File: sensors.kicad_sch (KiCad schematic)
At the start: 3 parts, among them IC5 BME690, U2 BME280, U3 BMP581

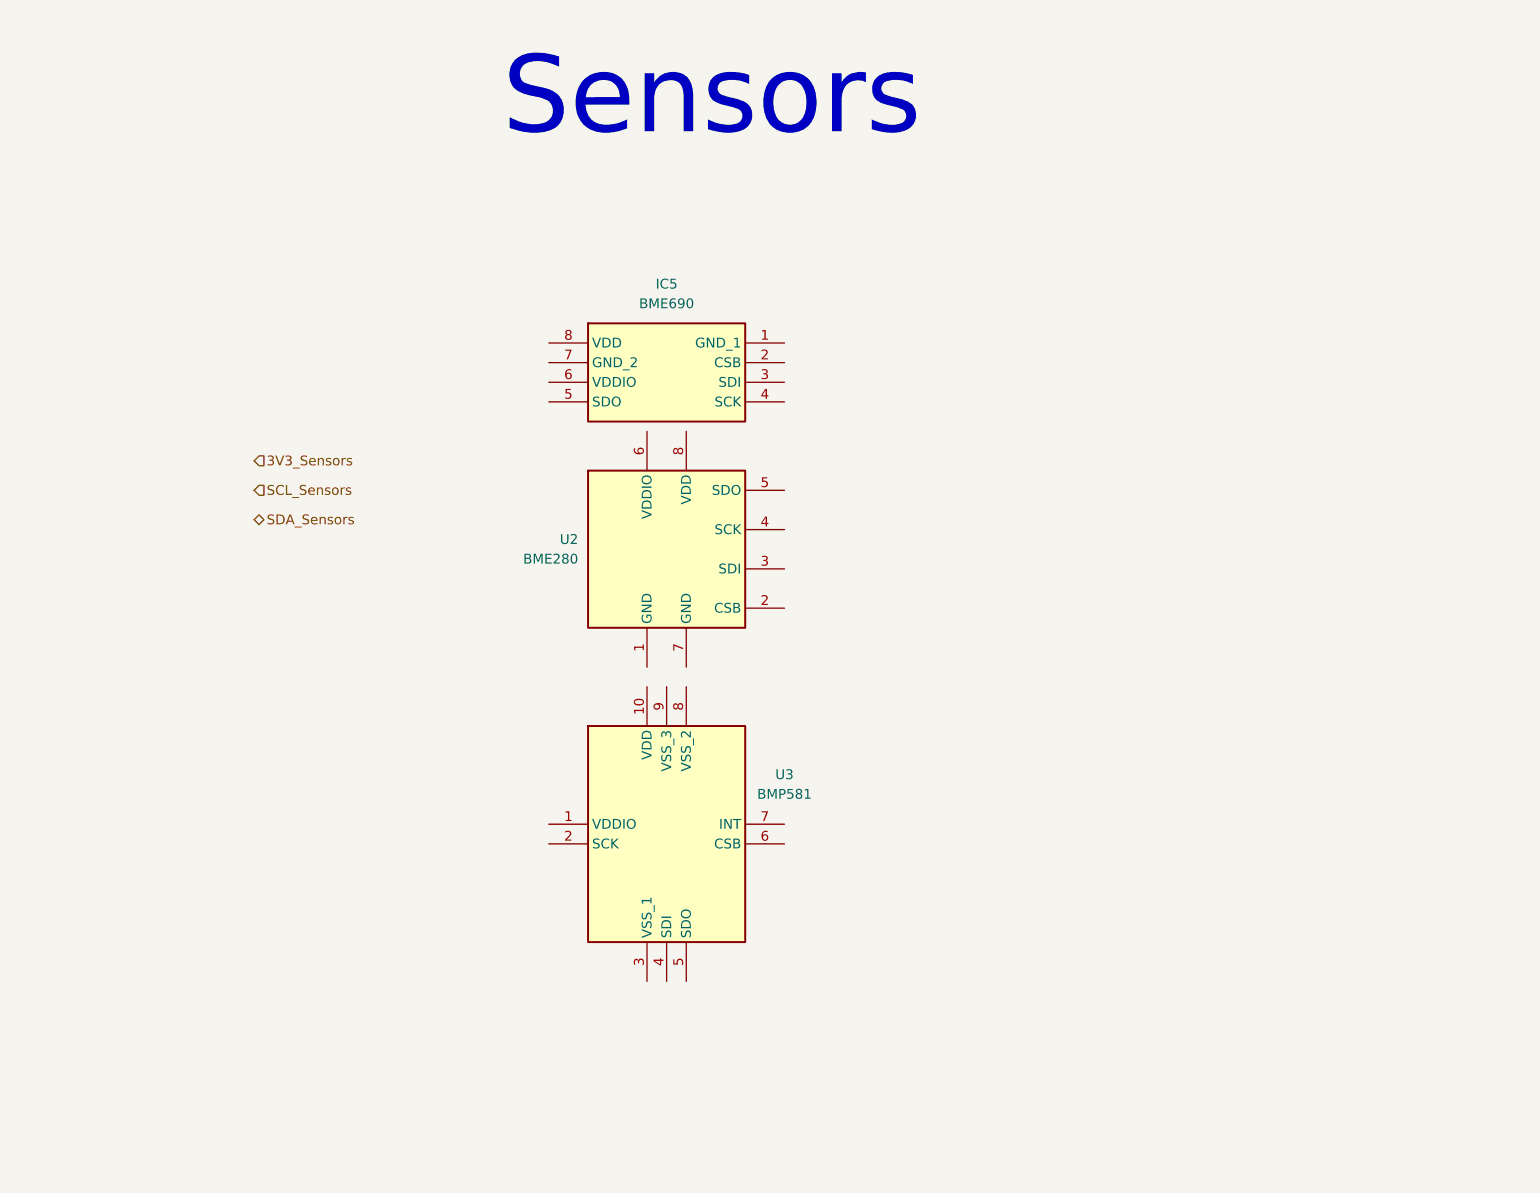
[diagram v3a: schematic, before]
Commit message: Cable all sensors
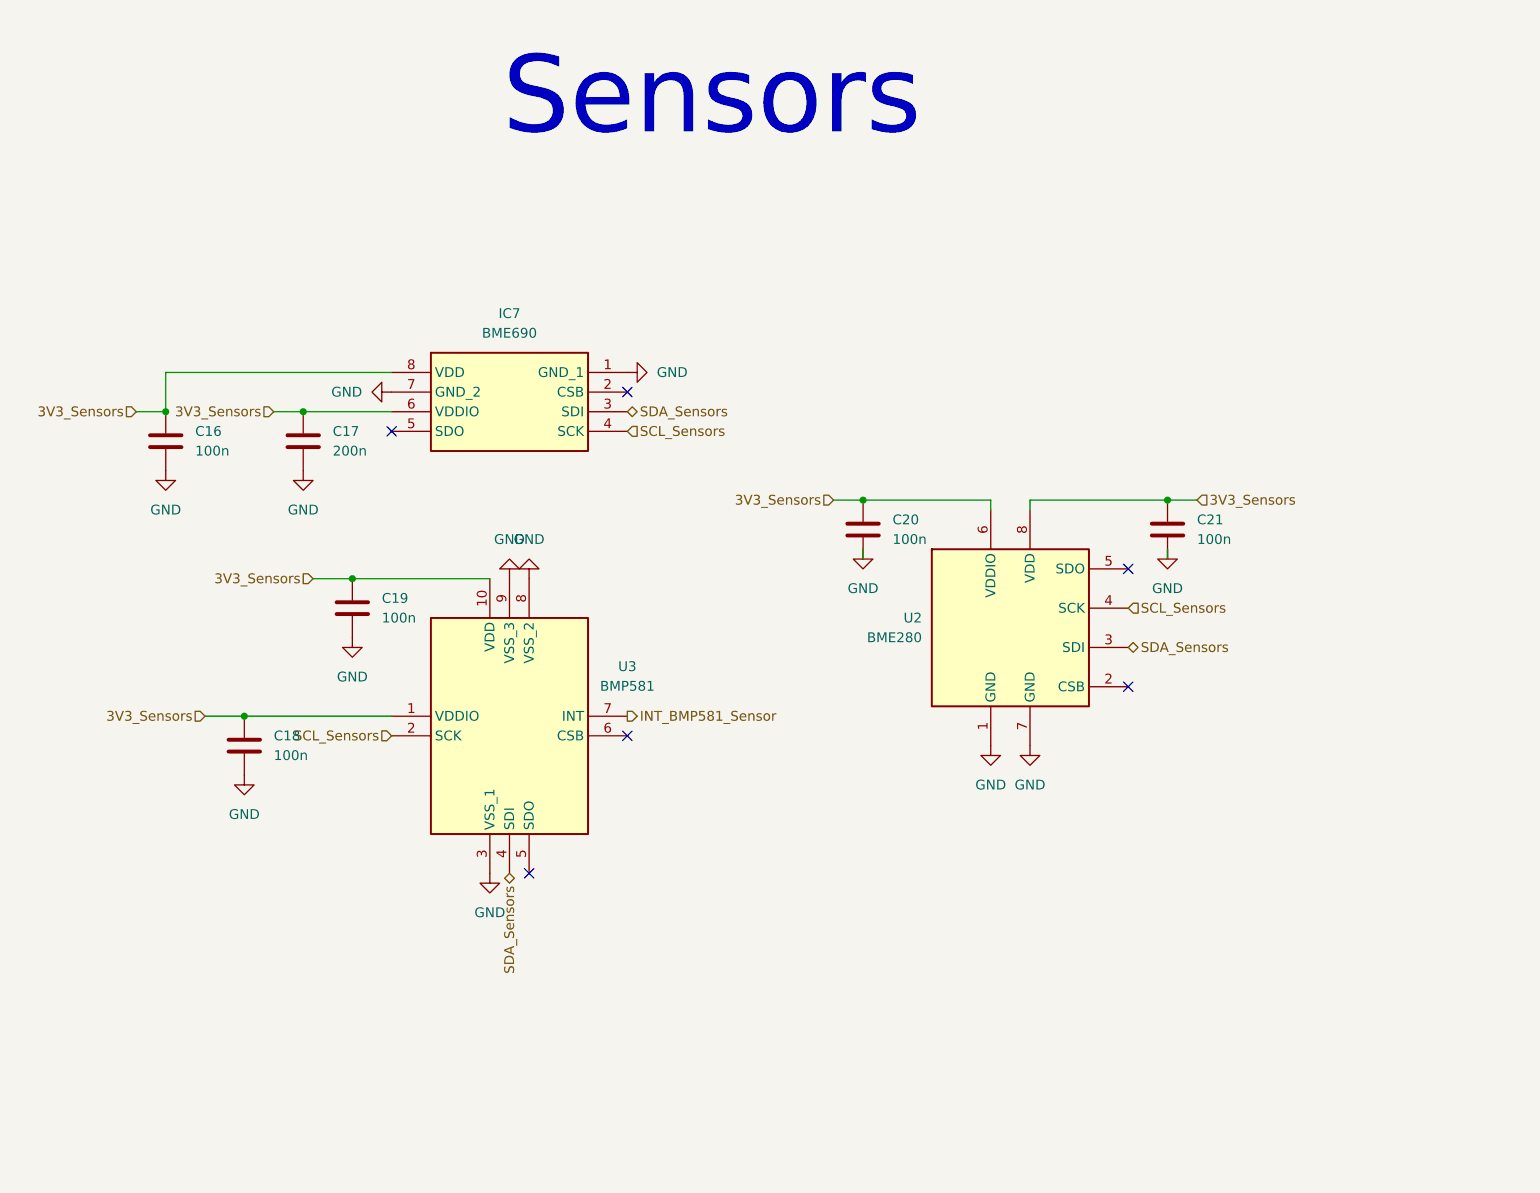
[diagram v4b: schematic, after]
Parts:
- removed IC5: BME690, BME690, symbol weather-station-poc-sym:BME690
- added C16, C18, C19, C20, C21: 100n, Capacitor_SMD:C_0402_1005Metric_Pad0.74x0.62mm_HandSolder, symbol Device:C
- added C17: 200n, Capacitor_SMD:C_0402_1005Metric_Pad0.74x0.62mm_HandSolder, symbol Device:C
- added IC7: BME690, BME690, symbol weather-station-poc-sym:BME690
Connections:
- net 3V3_Sensors: now also U2.6 (VDDIO), U2.8 (VDD), U3.1 (VDDIO), U3.10 (VDD), C16.1, C17.1, C18.1, C19.1, C20.1, C21.1, IC7.6 (VDDIO), IC7.8 (VDD)
- net SCL_Sensors: now also U2.4 (SCK), U3.2 (SCK), IC7.4 (SCK)
- net SDA_Sensors: now also U2.3 (SDI), U3.4 (SDI), IC7.3 (SDI)
- net GND: now reaches U3.3 (VSS_1)
- net GND: now also U2.1 (GND), U2.7 (GND), U3.8 (VSS_2), U3.9 (VSS_3), C16.2, C17.2, C18.2, C19.2, C20.2, C21.2, IC7.1 (GND_1), IC7.7 (GND_2)
- net INT_BMP581_Sensor: now reaches U3.7 (INT)
- no-connect marks 0 -> 6
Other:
- moved on the sheet: U2, U3

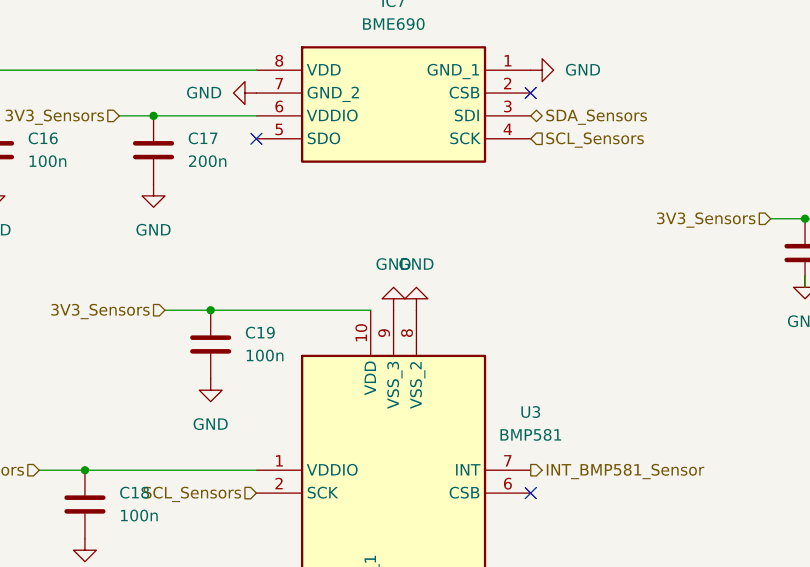
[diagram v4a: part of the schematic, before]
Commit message: Add S2LP schematic
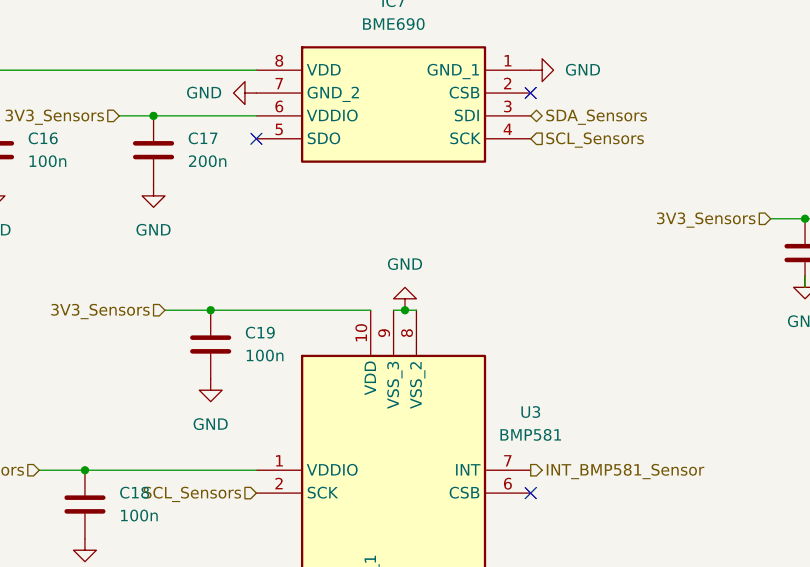
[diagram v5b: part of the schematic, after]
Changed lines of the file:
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@@
+	)
+	(junction
+		(at 124.46 88.9)
+		(diameter 0)
+		(color 0 0 0 0)
 	)
 	(junction
@@
 	(wire
 		(pts
+			(xy 124.46 88.9) (xy 125.73 88.9)
+		)
+		(stroke
+			(width 0)
+			(type default)
+		)
+	)
+	(wire
+		(pts
 			(xy 78.74 67.31) (xy 78.74 62.23)
 		)
@@
 		(pts
 			(xy 102.87 88.9) (xy 120.65 88.9)
+		)
+		(stroke
+			(width 0)
+			(type default)
+		)
+	)
+	(wire
+		(pts
+			(xy 123.19 88.9) (xy 124.46 88.9)
 		)
 		(stroke
@@
 	(symbol
 		(lib_id "power:GND")
-		(at 125.73 88.9 180)
-		(unit 1)
-		(exclude_from_sim no)
-		(in_bom yes)
-		(on_board yes)
-		(dnp no)
-		(fields_autoplaced yes)
-		(property "Reference" "#PWR043"
-			(at 125.73 82.55 0)
-			(effects
-				(font
-					(size 1.27 1.27)
-				)
-				(hide yes)
-			)
-		)
-		(property "Value" "GND"
-			(at 125.73 83.82 0)
-			(effects
-				(font
-					(size 1.27 1.27)
-				)
-			)
-		)
-		(property "Footprint" ""
-			(at 125.73 88.9 0)
-			(effects
-				(font
-					(size 1.27 1.27)
-				)
-				(hide yes)
-			)
-		)
-		(property "Datasheet" ""
-			(at 125.73 88.9 0)
-			(effects
-				(font
-					(size 1.27 1.27)
-				)
-				(hide yes)
-			)
-		)
-		(property "Description" "Power symbol creates a global label with name \"GND\" , ground"
-			(at 125.73 88.9 0)
-			(effects
-				(font
-					(size 1.27 1.27)
-				)
-				(hide yes)
-			)
-		)
-		(pin "1"
-		)
-		(instances
-			(project "weather-station-poc"
-				(path "/38eb53bb-294e-46e4-ad59-fd355ca373b9/29574217-d56b-4a63-a2c4-128dfec2758e"
-					(reference "#PWR043")
-					(unit 1)
-				)
-			)
-		)
-	)
-	(symbol
-		(lib_id "power:GND")
 		(at 190.5 110.49 0)
 		(unit 1)
@@
 	(symbol
 		(lib_id "power:GND")
-		(at 123.19 88.9 180)
+		(at 124.46 88.9 180)
 		(unit 1)
 		(exclude_from_sim no)
@@
 		(fields_autoplaced yes)
 		(property "Reference" "#PWR042"
-			(at 123.19 82.55 0)
+			(at 124.46 82.55 0)
 			(effects
 				(font
@@
 		)
 		(property "Value" "GND"
-			(at 123.19 83.82 0)
+			(at 124.46 83.82 0)
 			(effects
 				(font
@@
 		)
 		(property "Footprint" ""
-			(at 123.19 88.9 0)
+			(at 124.46 88.9 0)
 			(effects
 				(font
@@
 		)
 		(property "Datasheet" ""
-			(at 123.19 88.9 0)
+			(at 124.46 88.9 0)
 			(effects
 				(font
@@
 		)
 		(property "Description" "Power symbol creates a global label with name \"GND\" , ground"
-			(at 123.19 88.9 0)
-			(effects
-				(font
+			(at 124.46 88.9 0)
+			(effects
+				(font

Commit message: Fix warnings for footprint
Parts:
- IC7: footprint BME690 -> weather-station-poc-fp:BME690
- U3: footprint BMP581 -> weather-station-poc-fp:BMP581
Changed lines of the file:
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@@
 			)
 		)
-		(property "Footprint" "BMP581"
+		(property "Footprint" "weather-station-poc-fp:BMP581"
 			(at 134.62 191.44 0)
 			(effects
@@
 			)
 		)
-		(property "Footprint" "BME690"
+		(property "Footprint" "weather-station-poc-fp:BME690"
 			(at 134.62 157.15 0)
 			(effects

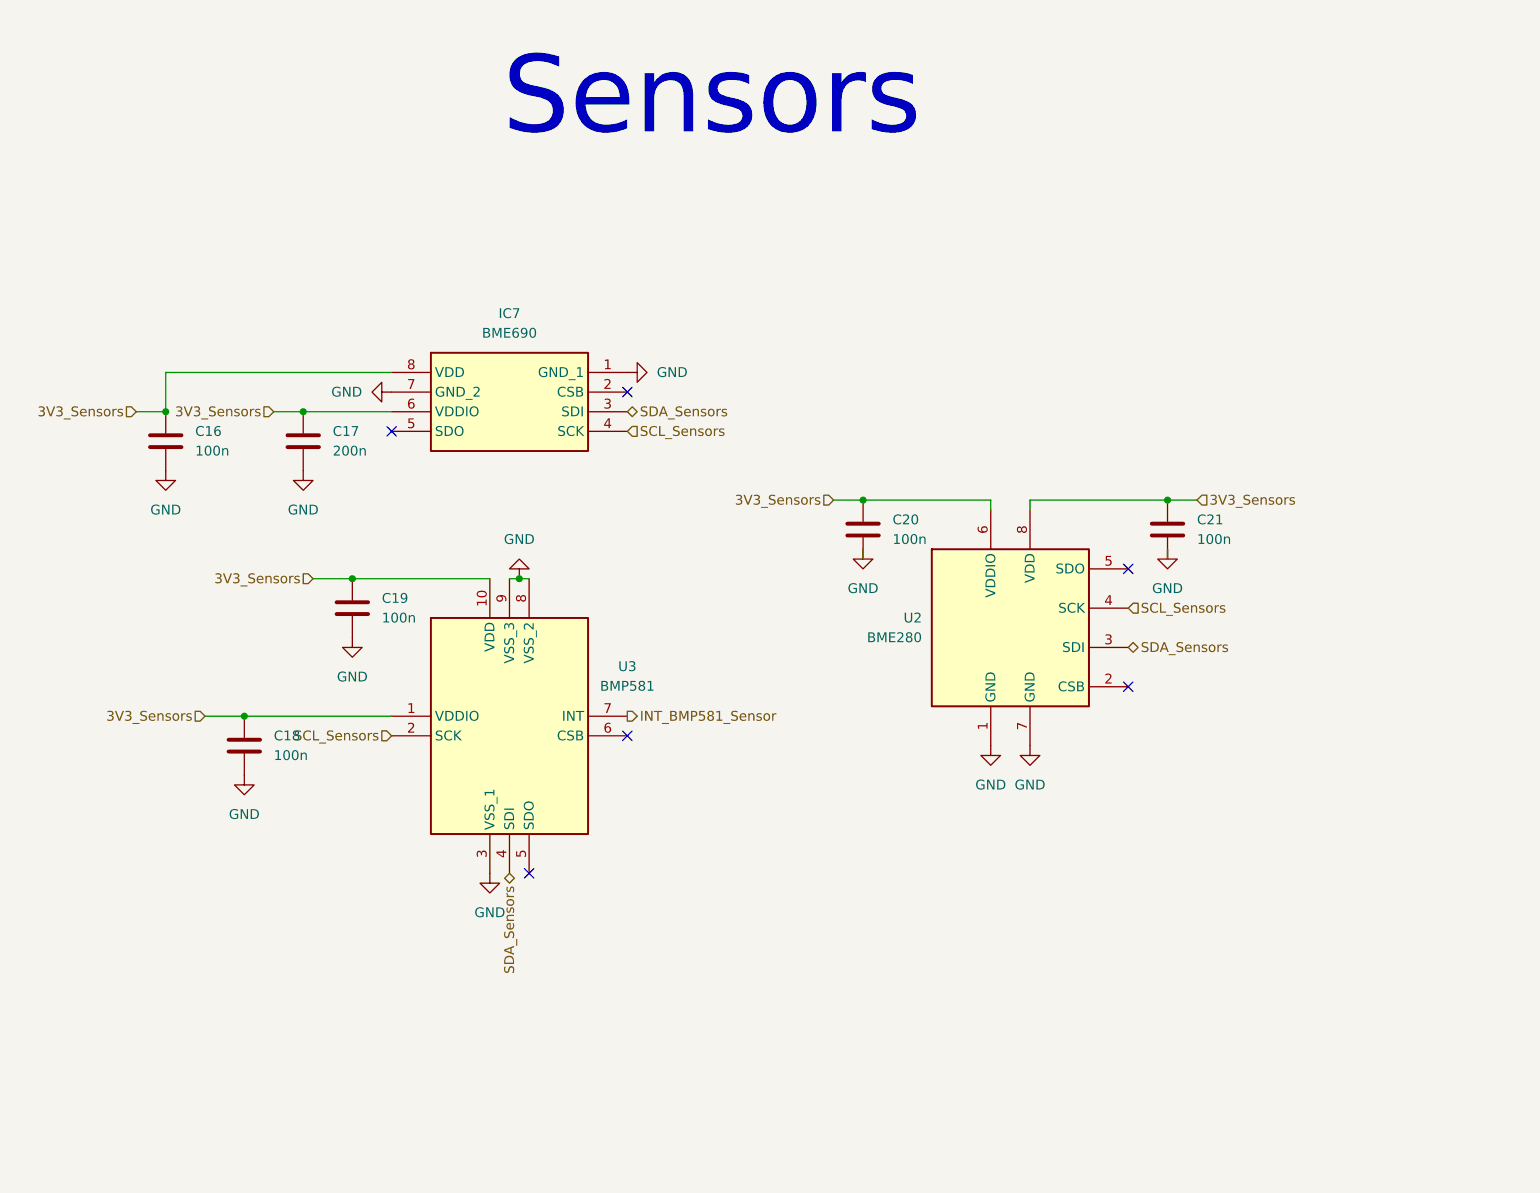
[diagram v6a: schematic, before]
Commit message: Functionnal block delimiting in schematics
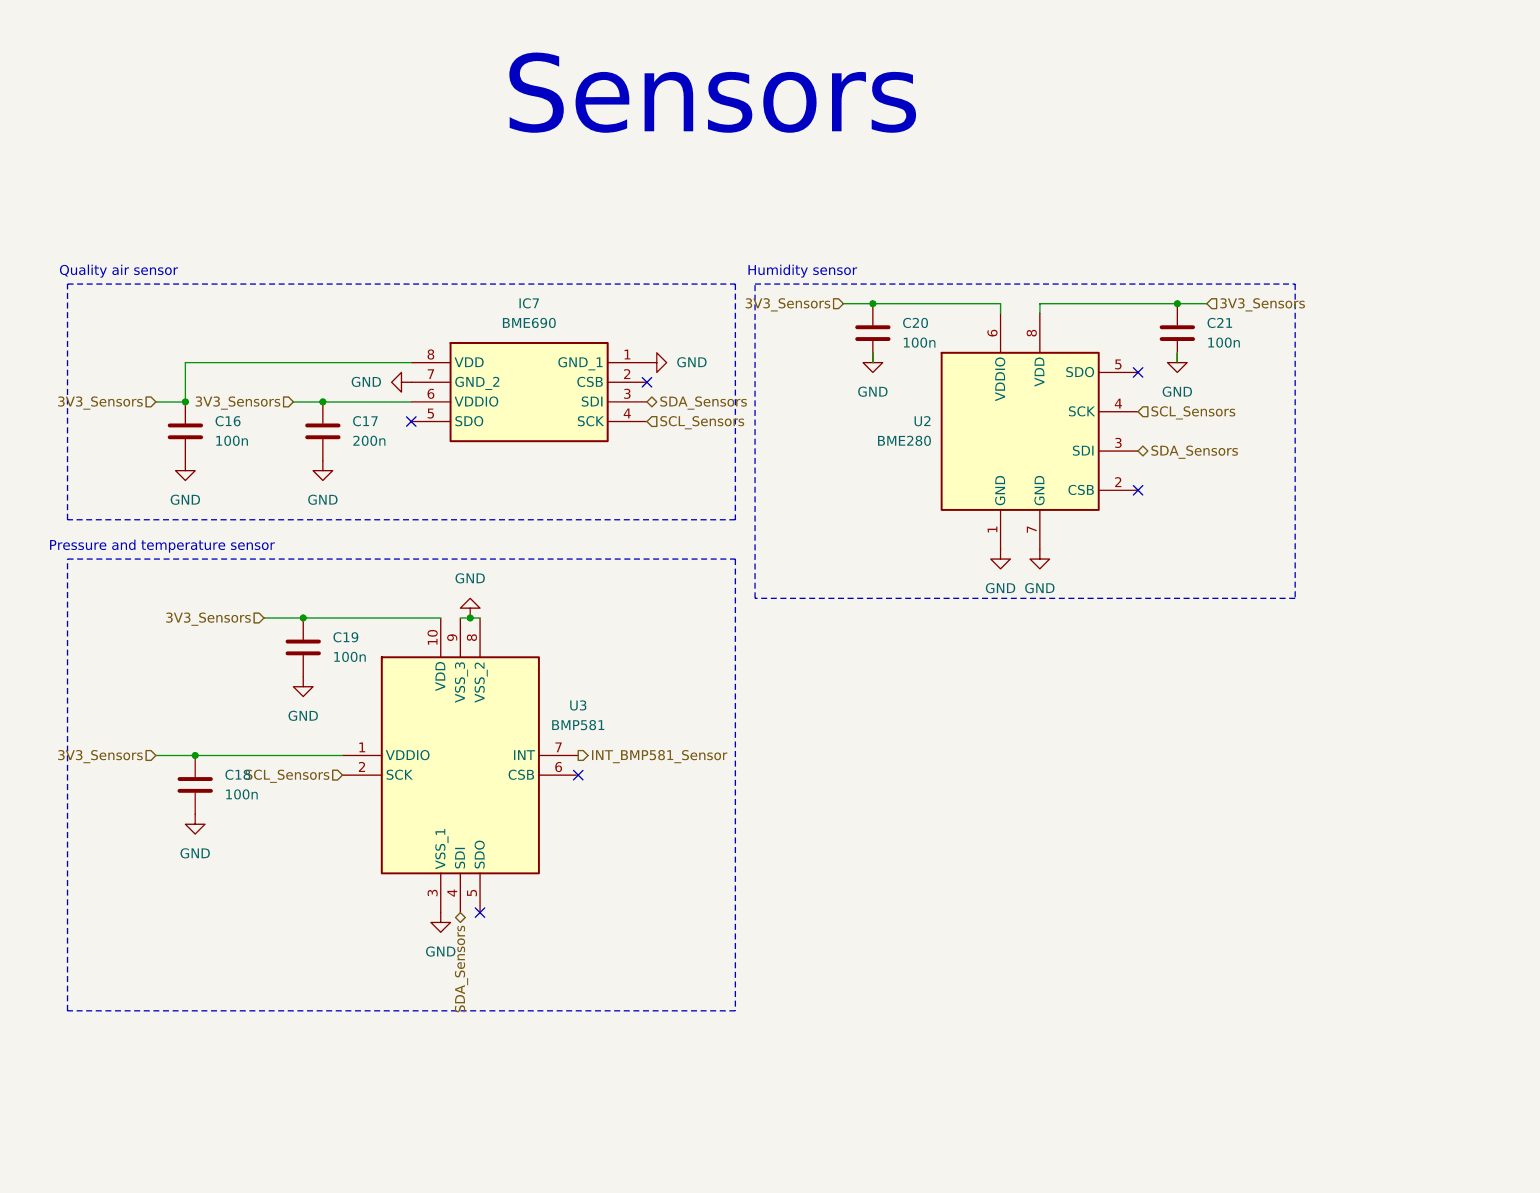
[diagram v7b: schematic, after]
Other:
- note added: "Humidity sensor"
- note added: "Pressure and temperature sensor"
- note added: "Quality air sensor"
- moved on the sheet: C16, C17, C18, C19, C20, C21, IC7, U2, U3
